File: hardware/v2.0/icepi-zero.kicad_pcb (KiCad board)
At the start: 4 copper layers, 65 x 30 mm, 165 parts, among them J1 Conn_02x20_Counter_Clockwise, J2 GPDI_C_1.3, J3 USB_C_Receptacle_USB2.0_14P, J4 USB_C_Receptacle_USB2.0_14P, J5 USB_C_Receptacle_USB2.0_14P, J6 Micro_SD_Card_Det2, SW1 SW_Push, SW2 SW_Push, U1 ECP5-CABGA256, U10 TPD2EUSB30A, U11 W9825G6KH, U12 W25Q128JVS, U2 TLV62569DBV, U3 TLV62569DBV, U4 TLV62569DBV, U5 TPD2EUSB30A, U6 PCA9306DC1, U7 TPD2EUSB30A, U8 TPD2EUSB30A, U9 FT231XQ, Y1 SG-8018CG 50.000000MHz

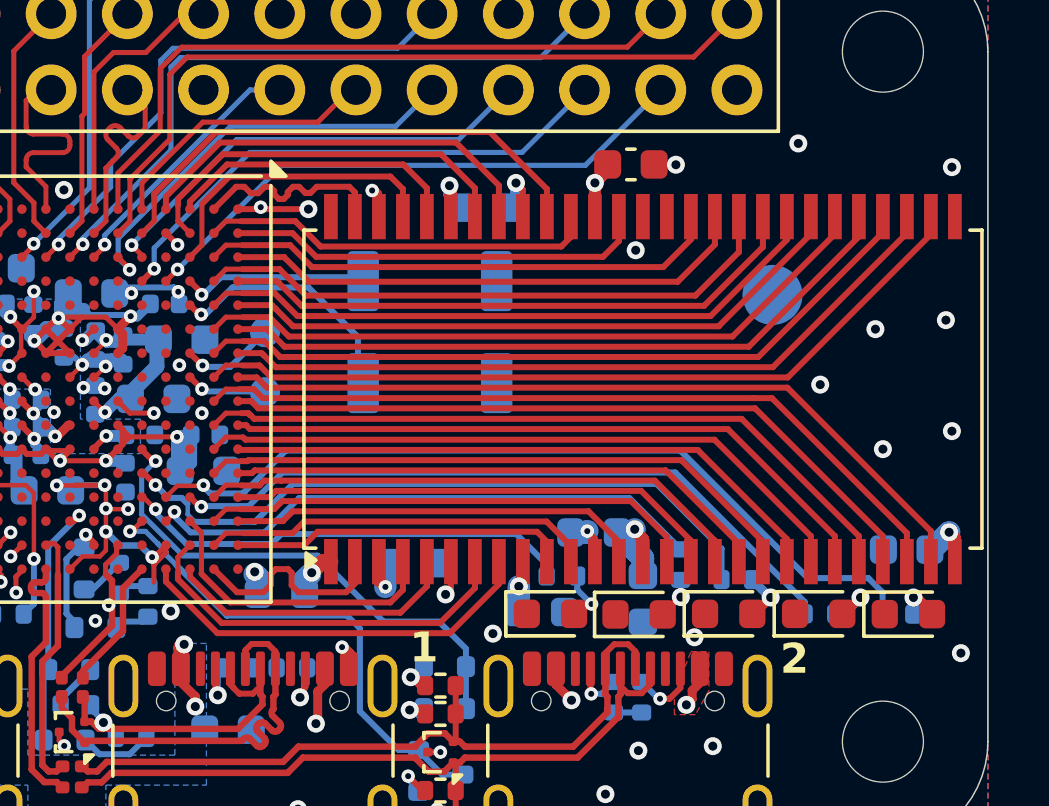
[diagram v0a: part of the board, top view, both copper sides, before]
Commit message: Added 54-TFPGA chip, front routing
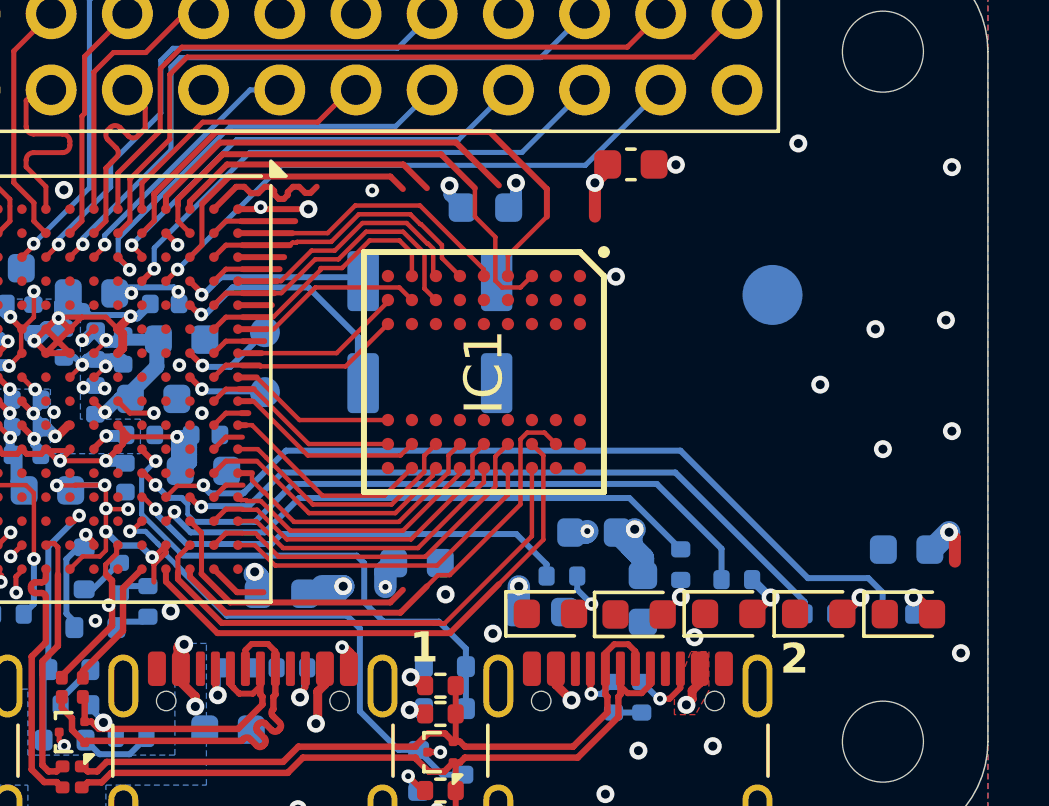
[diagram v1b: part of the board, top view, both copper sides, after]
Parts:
- removed U11: W9825G6KH, Package_SO:TSOP-II-54_22.2x10.16mm_P0.8mm
- added IC1: IS42S16160J-6BLI, IS42S16160J-6BLI:BGA54C80P9X9_800X800X120, F.Cu at (164.2, 104.2)
- L1, L2, L3: value 2.2uH 100mA+ 400mO- -> 2.2uH
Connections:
- net DONE renamed /Flash/DONE
- net INITN renamed /Flash/INITN
- net PROGRAMMING renamed /Flash/PROGRAMMING
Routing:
- net /SDRAM/A0: track 24.2 -> 1.34 mm
- net /SDRAM/A6: track 24.4 -> 1.83 mm
- net /SDRAM/BA1: track 22.3 -> 1.12 mm
- net /SDRAM/A3: track 26.2 -> 5.58 mm
- net /SDRAM/A4: track 26.2 -> 6.51 mm
- net /SDRAM/A9: track 20.7 -> 1.13 mm
- net /SDRAM/A2: track 26.3 -> 6.83 mm
- net /SDRAM/A5: track 24.3 -> 5.77 mm
- net /SDRAM/A1: track 24.2 -> 6.71 mm
- net /SDRAM/CKE: track 19.8 -> 2.34 mm
- net /SDRAM/~{CAS}: track 18.5 -> 1.14 mm
- net /SDRAM/A7: track 23.1 -> 6.55 mm
- net /SDRAM/CLK: track 17.7 -> 1.54 mm
- net /SDRAM/A10: track 22.3 -> 7.16 mm
- net /SDRAM/A8: track 22.5 -> 8.78 mm
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
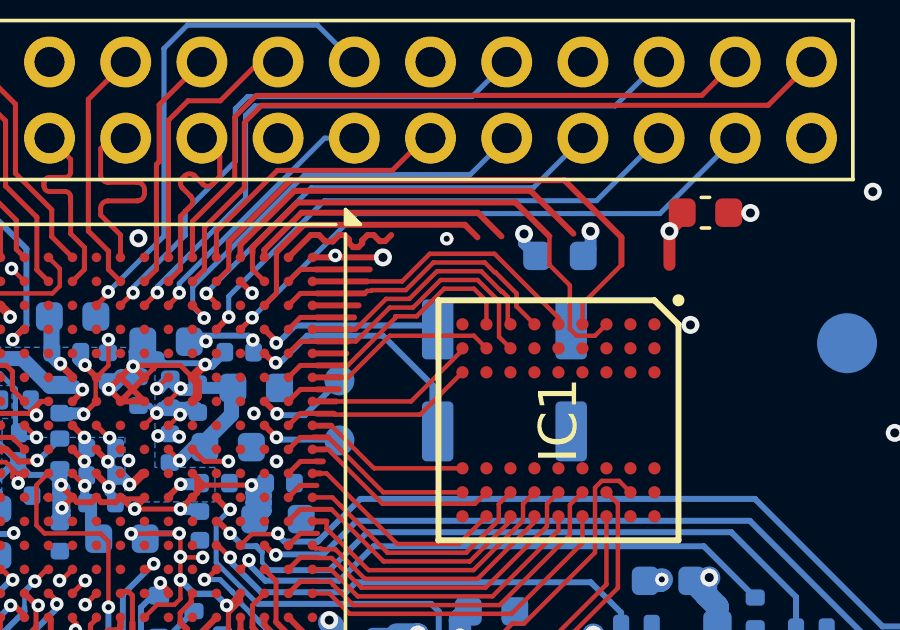
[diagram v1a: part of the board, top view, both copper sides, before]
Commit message: Front routing for memory chip
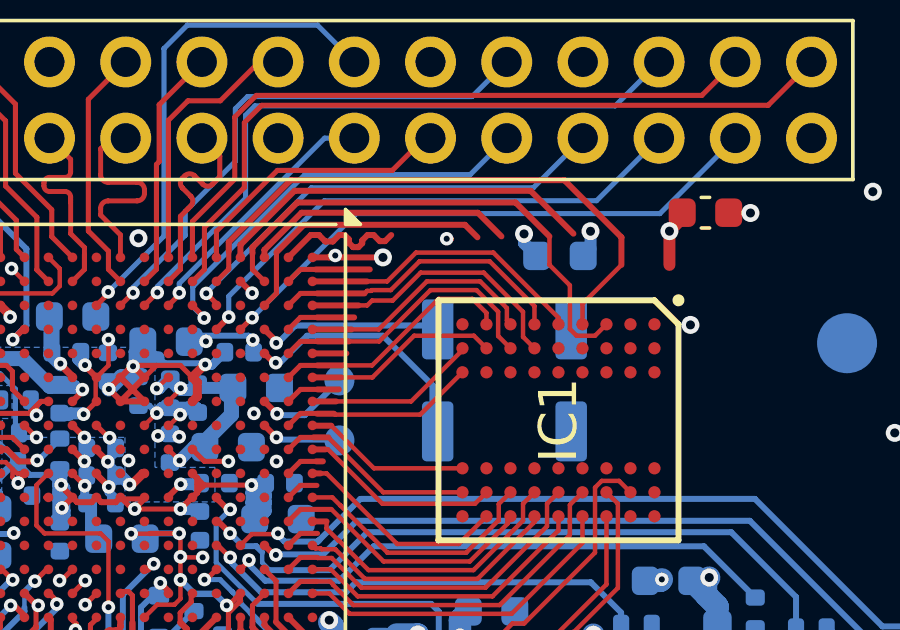
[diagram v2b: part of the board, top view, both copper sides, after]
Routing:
- net /SDRAM/CLK: track 1.54 -> 9.38 mm
- net /SDRAM/A8: track 8.78 -> 8.24 mm
- net /SDRAM/A11: track 10.1 -> 9.54 mm
- net /SDRAM/A12: track 8.62 -> 8.10 mm

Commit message: Front memory routs done
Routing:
- net /SDRAM/A0: track 1.34 -> 9.82 mm
- net /SDRAM/A6: track 1.83 -> 8.28 mm
- net /SDRAM/D9: track 2.86 -> 1.07 mm
- net /SDRAM/A7: track 6.55 -> 7.78 mm
- net /SDRAM/CKE: track 2.34 -> 1.12 mm
- net /SDRAM/A9: track 1.13 -> 0.00 mm

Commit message: Remaining memory routs
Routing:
- net /SDRAM/D9: track 1.07 -> 12.8 mm, vias 0 -> 2
- net /SDRAM/~{CAS}: track 1.14 -> 10.2 mm, vias 0 -> 2
- net /SDRAM/CKE: track 1.12 -> 10.1 mm, vias 0 -> 2
- net /SDRAM/A9: track 0.00 -> 7.87 mm, vias 0 -> 2
- net /SDRAM/BA1: track 1.12 -> 8.77 mm, vias 0 -> 2
- net /SDRAM/D15: track 4.55 -> 0.00 mm
- net /SW0: track 5.93 -> 6.75 mm

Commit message: Remaining memory data lines done
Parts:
- moved C52 1.77 mm to (166.0, 98.7)
- moved C49 1.00 mm to (158.2, 111.0)
- moved C47 0.59 mm to (162.6, 110.5)
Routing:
- net /SDRAM/D15: track 0.00 -> 16.5 mm, vias 0 -> 2
- net /SDRAM/D0: track 1.97 -> 17.5 mm, vias 0 -> 2
- net /SDRAM/D13: track 8.99 -> 17.3 mm, vias 0 -> 2
- net /SDRAM/D1: track 9.20 -> 16.6 mm, vias 0 -> 2
- net /SDRAM/D14: track 9.17 -> 16.3 mm, vias 0 -> 2
- net /SDRAM/D11: track 12.9 -> 17.8 mm, vias 0 -> 2
- net +3V3: track 93.0 -> 89.8 mm
- net /SDRAM/D10: track 19.6 -> 18.0 mm
- net GND: track 102.4 -> 103.4 mm
- net /USB/USB1_PULL_D-: track 18.0 -> 17.4 mm
